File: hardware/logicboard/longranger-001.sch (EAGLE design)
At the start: 25 parts, among them IC1 74LS07N, IC2 LTC485N, IC3 LTC485N

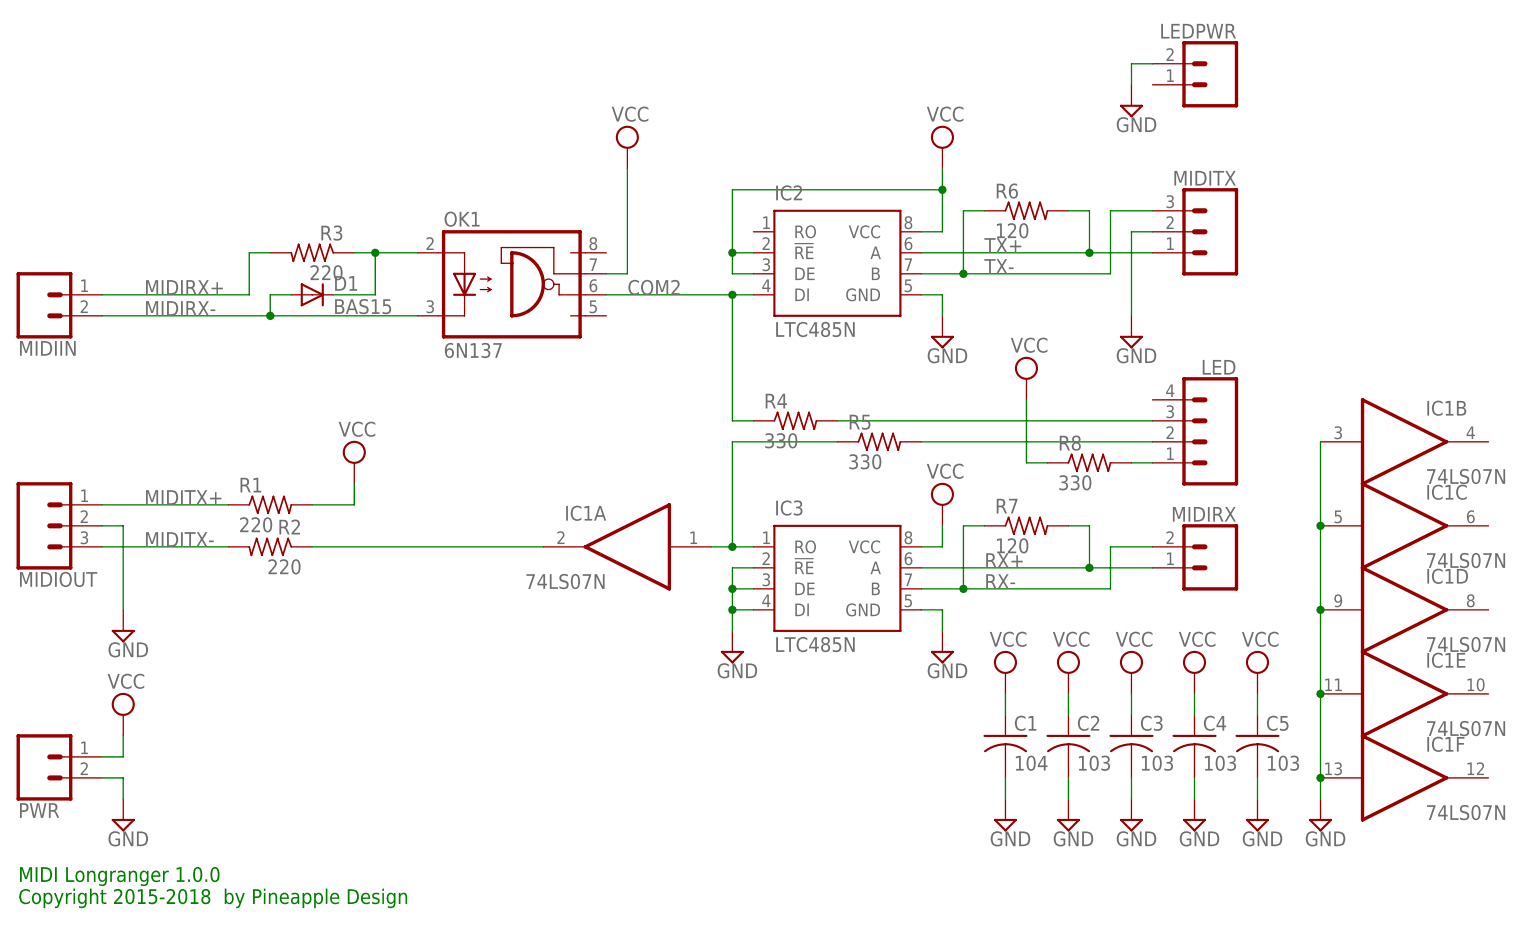
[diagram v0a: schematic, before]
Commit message: New front panel.
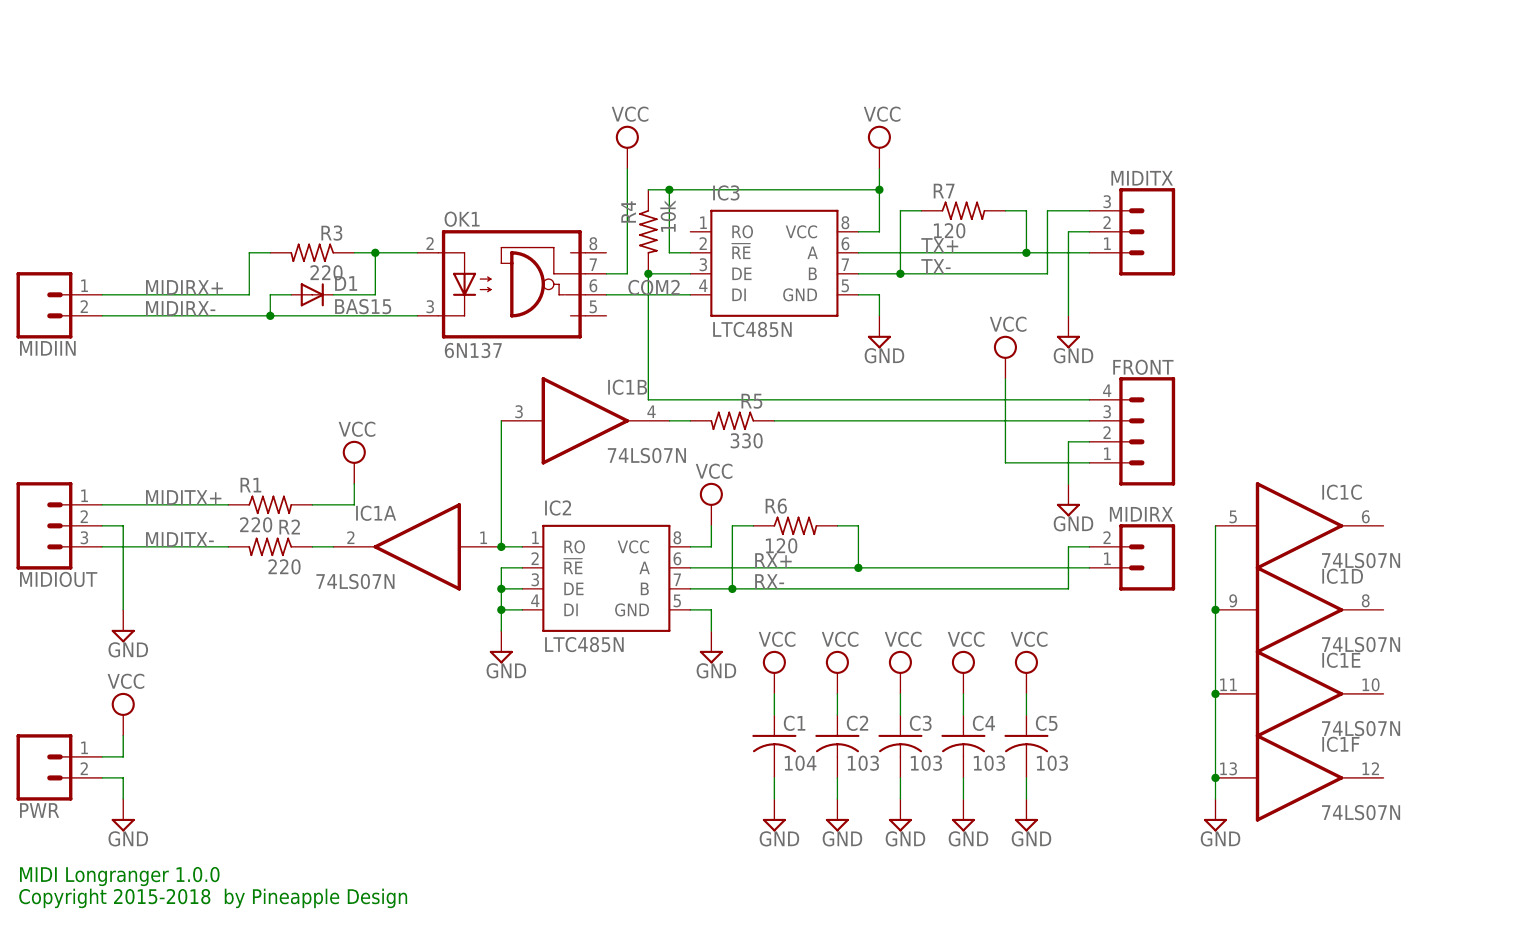
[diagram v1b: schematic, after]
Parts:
- removed LED: (no value), SparkFun-Connectors:CONN_04JST-PTH
- removed LEDPWR: (no value), SparkFun-Connectors:CONN_02JST-PTH-2
- removed R8: 330, resistor:R-US_0204/5
- added FRONT: (no value), SparkFun-Connectors:CONN_04JST-PTH
- R4: value 330 -> 10k
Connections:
- removed net N$5: LED.3, R4.2
- new net N$6: FRONT.4, IC3.DE, R4.2
- net COM2: now also IC3.DI; no longer IC2.DI, R4.1
- net GND: now also FRONT.2, IC2.!RE, IC2.DE, IC2.DI; no longer IC1B.I, IC3.!RE, IC3.DE, IC3.DI, LEDPWR.2
- net N$1: now also IC1B.I, IC2.RO; no longer IC3.RO, R5.1
- net N$3: now also IC1B.O, R5.2; no longer LED.1, R8.2
- net N$4: now also FRONT.3, R5.1; no longer LED.2, R5.2
- net RX+: now also IC2.A, R6.2; no longer IC3.A, R7.2
- net RX-: now also IC2.B, R6.1; no longer IC3.B, R7.1
- net TX+: now also IC3.A, R7.2; no longer IC2.A, R6.2
- net TX-: now also IC3.B, R7.1; no longer IC2.B, R6.1
- net VCC: now also FRONT.1, IC3.!RE, R4.1; no longer IC2.!RE, IC2.DE, R8.1
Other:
- moved on the sheet: C1, C2, C3, C4, C5, IC1A, IC1B, IC1C, IC1D, IC1E, IC1F, IC2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

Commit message: Changed signal name.
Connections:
- net N$1 renamed COM1
- net N$4 renamed INDICATOR
- net N$6 renamed MUTE
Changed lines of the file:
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@@
 <setting verticaltext="up"/>
 </settings>
-<grid distance="0.1" unitdist="inch" unit="inch" style="lines" multiple="1" display="no" altdistance="0.01" altunitdist="inch" altunit="inch"/>
+<grid distance="0.1" unitdist="inch" unit="inch" style="lines" multiple="1" display="yes" altdistance="0.01" altunitdist="inch" altunit="inch"/>
 <layers>
 <layer number="1" name="Top" color="4" fill="1" visible="no" active="no"/>
@@
 <pinref part="IC2" gate="G$1" pin="A"/>
 <wire x1="83.82" y1="43.18" x2="104.14" y2="43.18" width="0.1524" layer="91"/>
-<label x="91.44" y="43.18" size="1.778" layer="95"/>
+<label x="111.76" y="43.18" size="1.778" layer="95"/>
 <wire x1="104.14" y1="43.18" x2="132.08" y2="43.18" width="0.1524" layer="91"/>
 <junction x="104.14" y="43.18"/>
@@
 <wire x1="88.9" y1="48.26" x2="88.9" y2="40.64" width="0.1524" layer="91"/>
 <wire x1="88.9" y1="40.64" x2="83.82" y2="40.64" width="0.1524" layer="91"/>
-<label x="91.44" y="40.64" size="1.778" layer="95"/>
+<label x="111.76" y="40.64" size="1.778" layer="95"/>
 <wire x1="132.08" y1="45.72" x2="129.54" y2="45.72" width="0.1524" layer="91"/>
 <wire x1="129.54" y1="45.72" x2="129.54" y2="40.64" width="0.1524" layer="91"/>
@@
 <pinref part="OK1" gate="A" pin="VO"/>
 <wire x1="73.66" y1="76.2" x2="83.82" y2="76.2" width="0.1524" layer="91"/>
-<label x="76.2" y="76.2" size="1.778" layer="95"/>
 <pinref part="IC3" gate="G$1" pin="DI"/>
 </segment>
@@
 </segment>
 </net>
-<net name="N$1" class="0">
+<net name="COM1" class="0">
 <segment>
 <pinref part="IC2" gate="G$1" pin="RO"/>
@@
 </segment>
 </net>
-<net name="N$4" class="0">
+<net name="INDICATOR" class="0">
 <segment>
 <pinref part="FRONT" gate="G$1" pin="3"/>
 <pinref part="R5" gate="G$1" pin="1"/>
 <wire x1="132.08" y1="60.96" x2="93.98" y2="60.96" width="0.1524" layer="91"/>
-</segment>
-</net>
-<net name="N$6" class="0">
+<label x="111.76" y="60.96" size="1.778" layer="95"/>
+</segment>
+</net>
+<net name="MUTE" class="0">
 <segment>
 <pinref part="IC3" gate="G$1" pin="DE"/>
@@
 <pinref part="FRONT" gate="G$1" pin="4"/>
 <wire x1="78.74" y1="63.5" x2="132.08" y2="63.5" width="0.1524" layer="91"/>
-</segment>
-</net>
+<label x="111.76" y="63.5" size="1.778" layer="95"/>
+</segment>
+</net>
